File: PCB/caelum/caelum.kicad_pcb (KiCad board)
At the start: 2 copper layers, 54 x 39.5 mm, 26 parts, among them J1 Conn_01x06_Pin, J10 Conn_01x04_Pin, J3 Pulse1, J4 Batt, J6 Pulse2, J7 Conn_01x04_Pin, J8 DS18B20, Q1 FS8205A-FC, U1 DW01A, U2 MCP1700T-3302E, U3 ESP32-H2-SUPERMINI

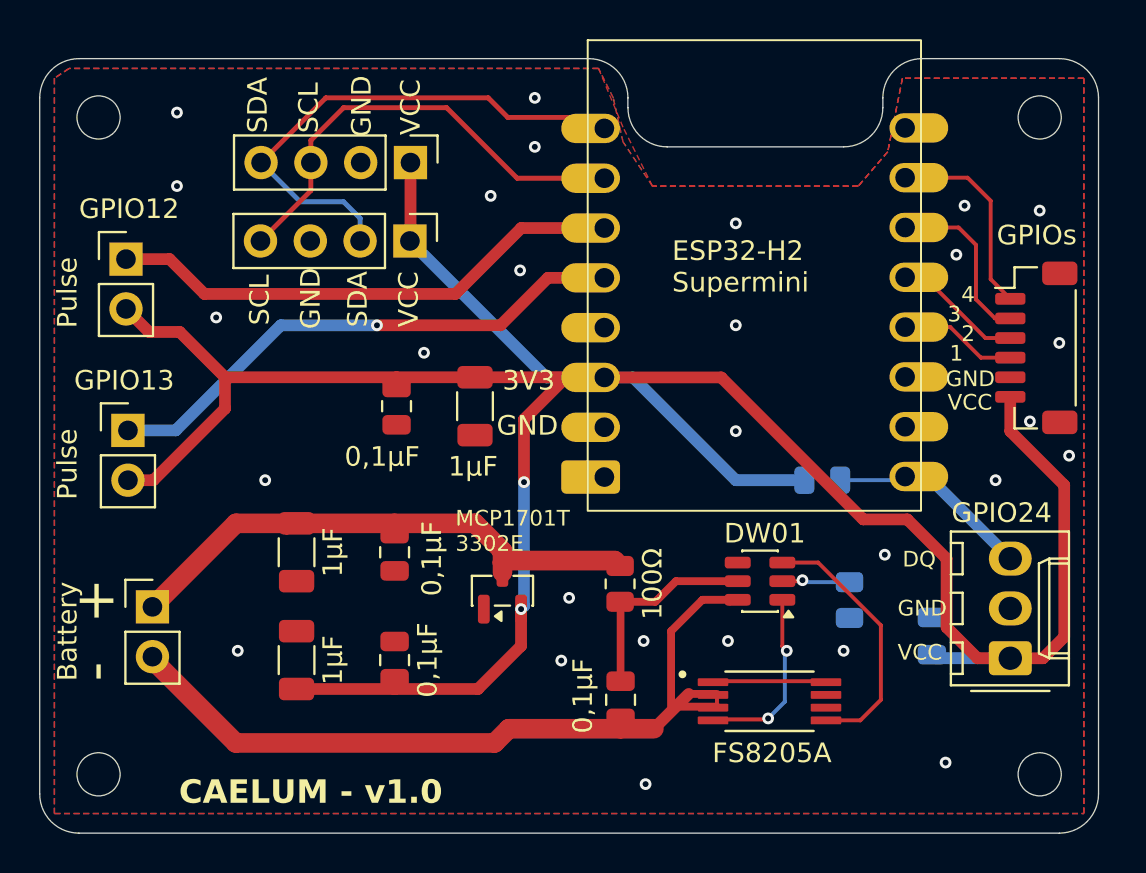
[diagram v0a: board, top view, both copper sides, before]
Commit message: feat: Enhance Caelum Weather Station functionality and configuration
- Updated PCB configuration to set active layer to 0 and adjusted column widths for better layout.
- Expanded device endpoints in the weather station to include additional sensors (pulse counter and temperature).
- Implemented sleep prevention during initial network configuration to ensure proper reporting setup.
- Added logic to load and save pulse counter data to RTC and NVS for persistence across power cycles.
- Improved DS18B20 sensor initialization with retry logic for better reliability.
- Enhanced logging for various operations to provide clearer insights during execution.
- Updated SDK configuration for flash settings and memory management.
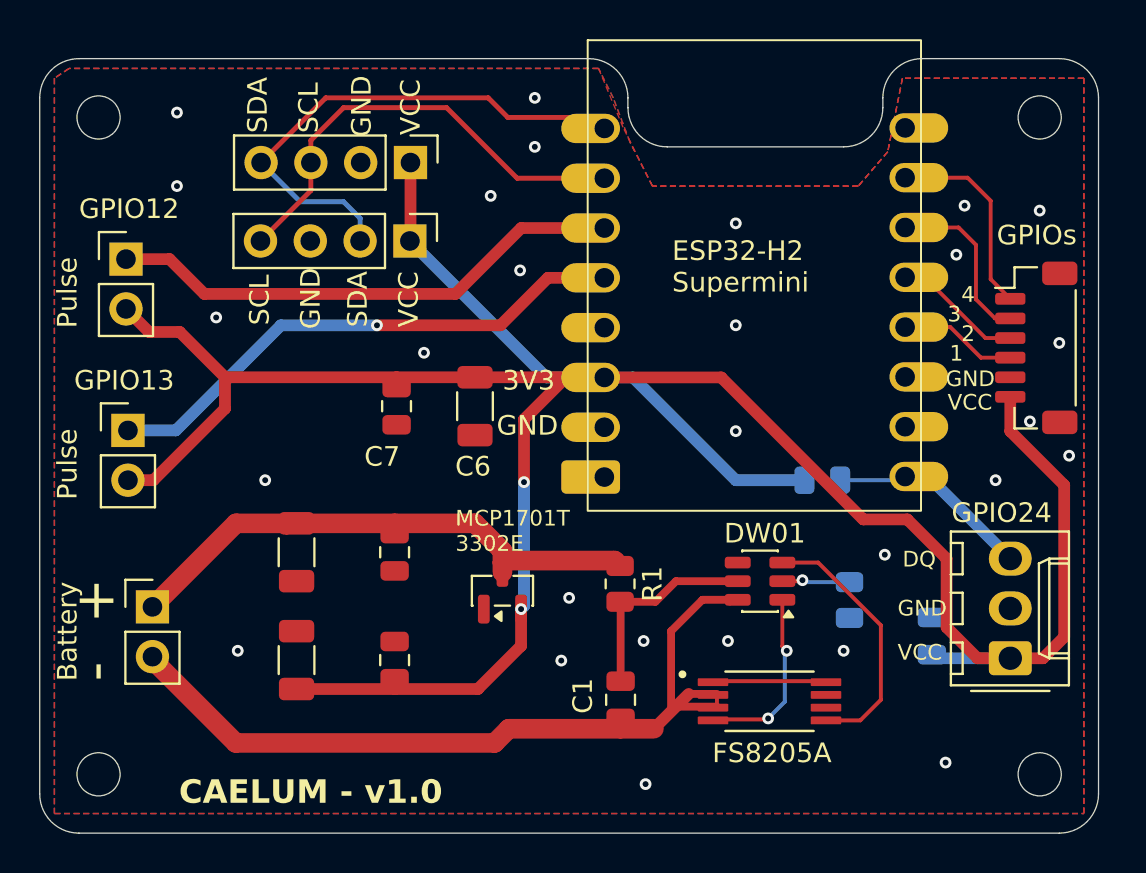
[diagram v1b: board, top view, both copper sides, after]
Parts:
- R3: value 4.7KΩ -> 4.7K
- renumbered 0,1µF to C1, 1µF to C2, 0,1µF to C3, 1µF to C4, 0,1µF to C5, 1µF to C6, 0,1µF to C7, 0,1µF to C8, 100Ω to R1, 1KΩ to R2
